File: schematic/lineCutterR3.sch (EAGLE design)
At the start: 60 parts, among them J1 10118192-0001LF, Q1 AO4576, Q2 AO4576, Q4 AO4576, Q5 DMG2305, SW1 KMR2, U1 MS560702BA03-50, U2 MDBT50Q, U3 S25FL128SDPMFIG13S03016, U4 ACS711KEXLT-31AB-T, U6 ICM-20602, X1 2x5 0.05"

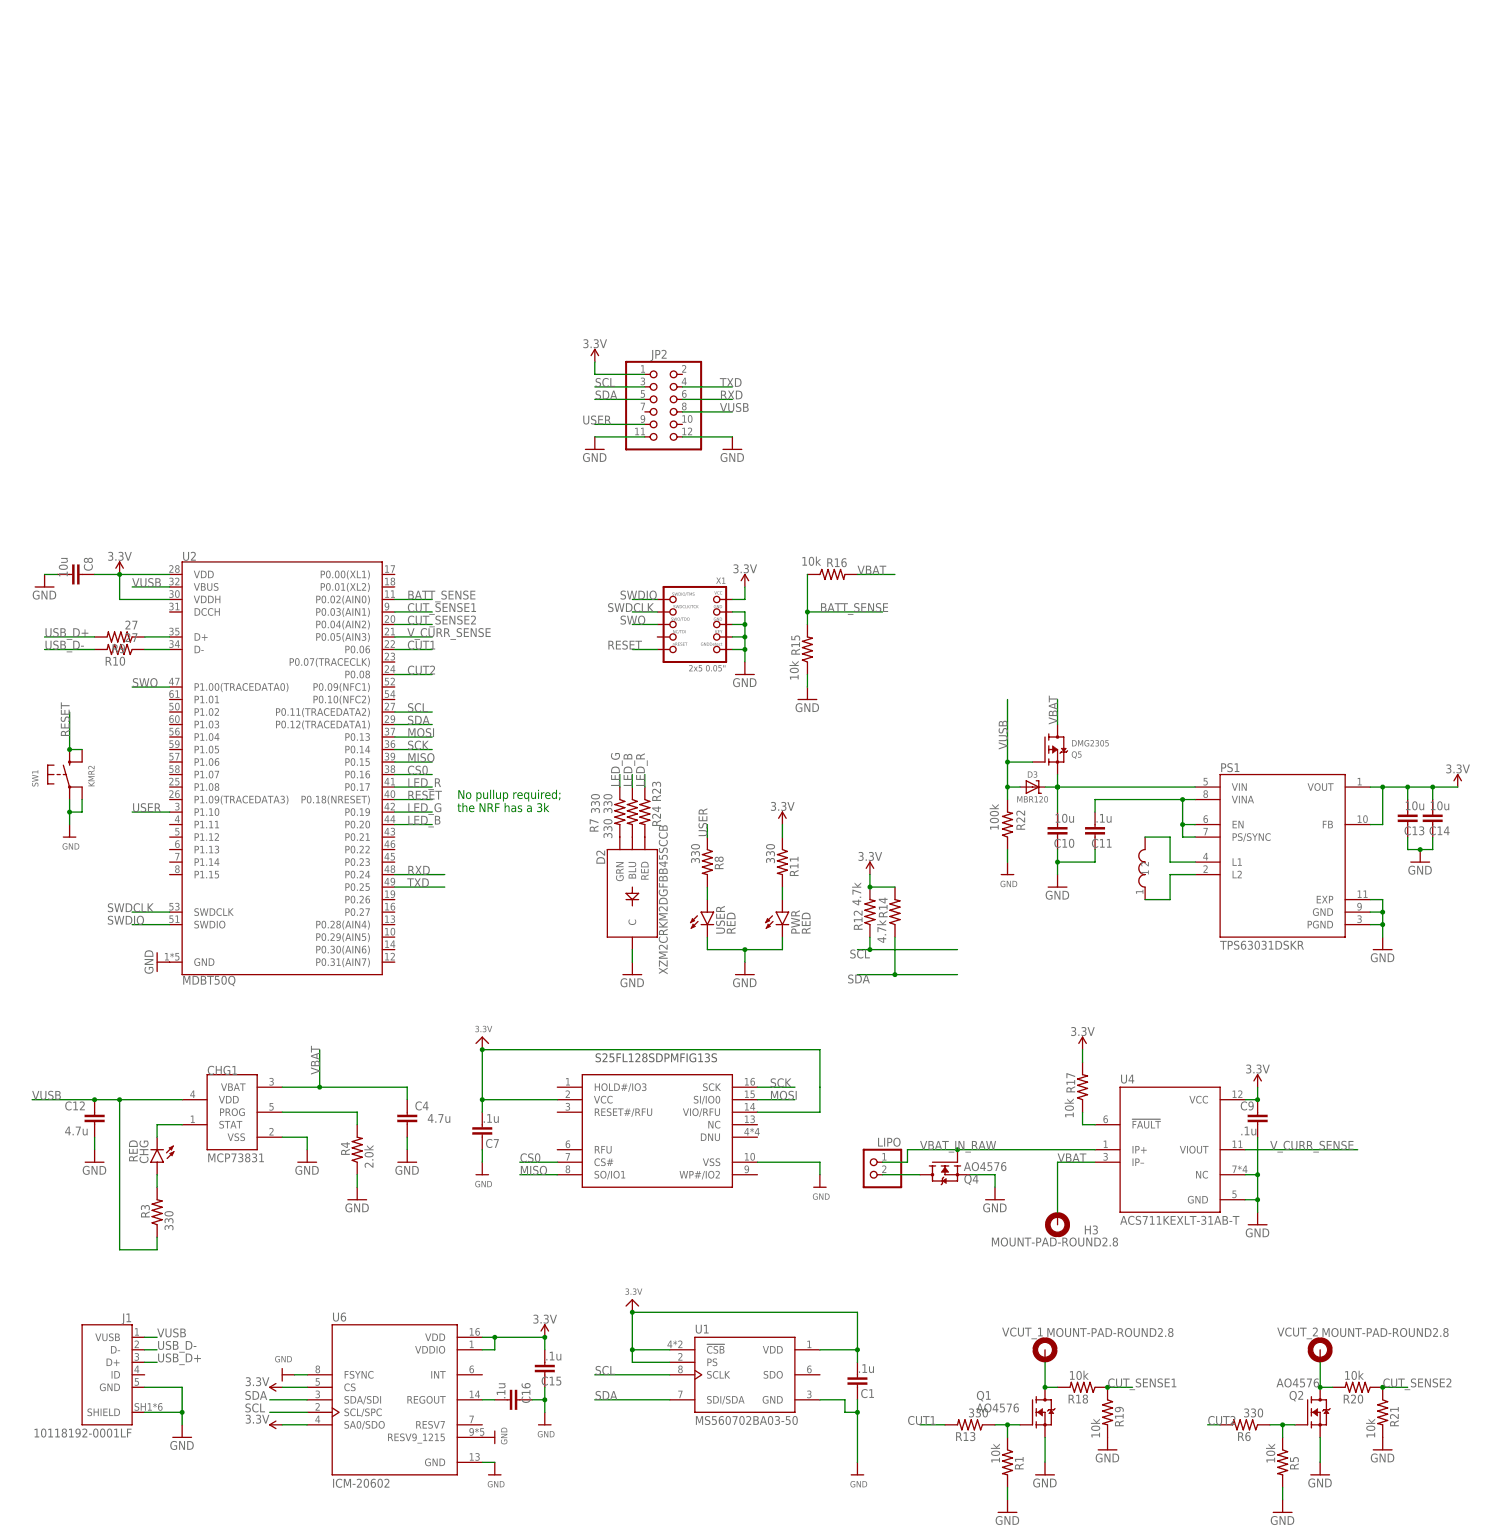
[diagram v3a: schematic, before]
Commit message: Switch back to 3v3 lin reg
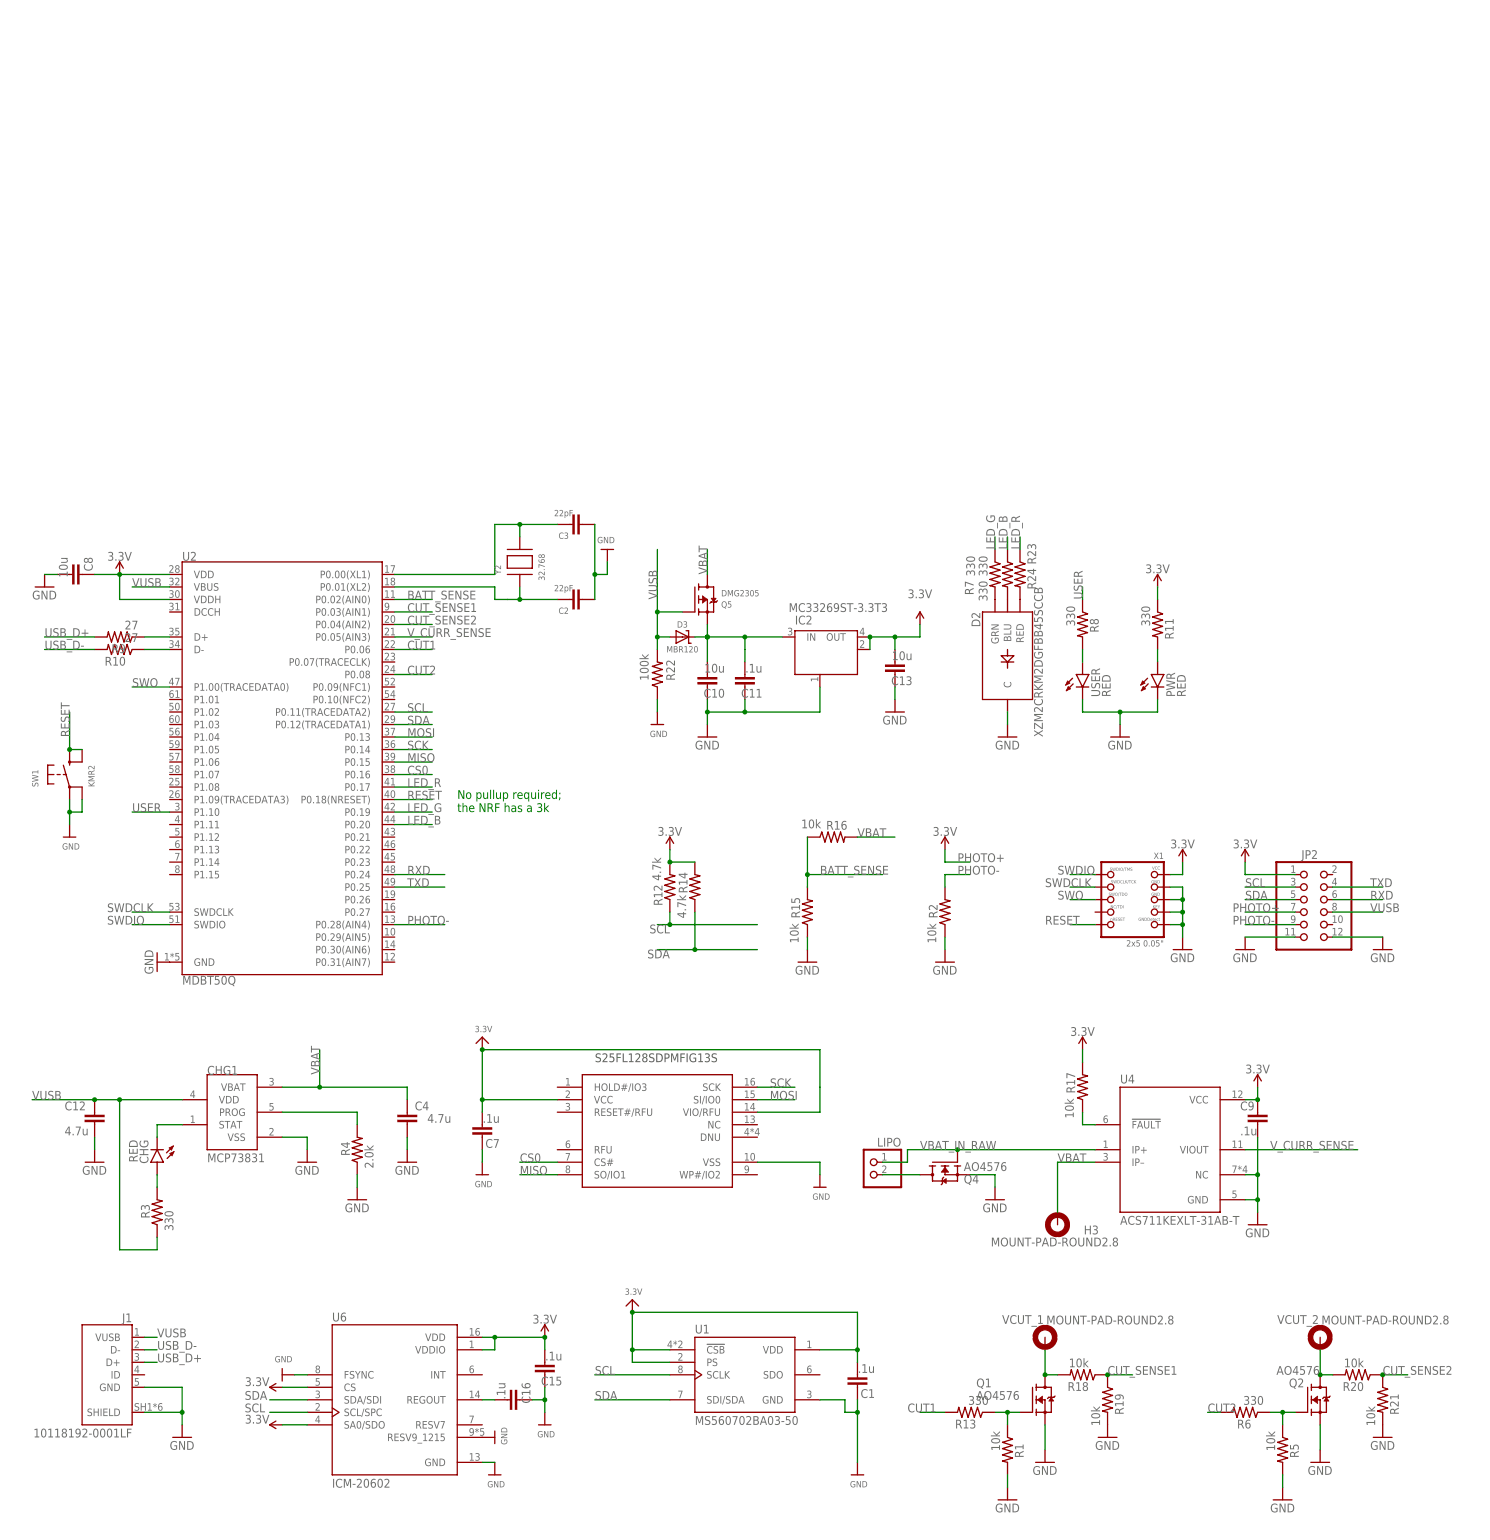
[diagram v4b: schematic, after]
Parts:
- removed C14: 10u, rcl:C-EUC0805
- removed L1: NR3015T1R5N, Line Cutter COTS:NR3015T1R5N
- removed PS1: TPS63031DSKR, Line Cutter COTS:TPS63031DSKR
- added C2, C3: 22pF, rcl:C-EUC0805
- added IC2: MC33269ST-3.3T3, linear:MC33269ST-3.3T3
- added R2: 10k, rcl:R-US_R0805
- added Y2: 32.768, adafruit2:XTAL-3.2X1.5
- H3, VCUT_1, VCUT_2: device holes:MOUNT-PAD-ROUND2.8 -> Line Cutter COTS:MOUNT-PAD-ROUND2.8
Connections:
- removed net N$18: C11.2, PS1.EN, PS1.PS/SYNC, PS1.VINA
- removed net N$19: L1.2, PS1.L1
- removed net N$20: L1.1, PS1.L2
- new net N$13: C3.1, U2.P0.00(XL1), Y2.P$2
- new net N$2: C2.1, U2.P0.01(XL2), Y2.P$1
- new net PHOTO+: JP2.7
- new net PHOTO-: JP2.9, R2.2, U2.P0.28(AIN4)
- net 3.3V: now also IC2.OUT, IC2.OUT@1; no longer C14.2, PS1.FB, PS1.VOUT
- net GND: now also C2.2, C3.2, IC2.GND/ADJ, R2.1; no longer C14.1, PS1.EXP, PS1.GND, PS1.PGND
- net USER: no longer JP2.9
- net VIN_REG1: now also C11.2, IC2.IN; no longer PS1.VIN
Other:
- moved on the sheet: C10, C11, C13, D2, D3, JP2, PWR, Q1, Q2, Q5, R1, R11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

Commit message: Final board stuff
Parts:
- U4: value ACS711KEXLT-31AB-T -> ACS711KEXLT-15AB-T
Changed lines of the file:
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@@
 <part name="GND22" library="supply1" library_urn="urn:adsk.eagle:library:371" deviceset="GND" device=""/>
 <part name="SUPPLY10" library="SparkFun-PowerSymbols" deviceset="3.3V" device=""/>
-<part name="U4" library="Line Cutter COTS" deviceset="ACS711KEXLT-31AB-T" device=""/>
+<part name="U4" library="Line Cutter COTS" deviceset="ACS711KEXLT-31AB-T" device="" value="ACS711KEXLT-15AB-T"/>
 <part name="D2" library="SparkFun-LED" deviceset="SUNLED" device="SMD1" value="XZM2CRKM2DGFBB45SCCB"/>
 <part name="GND7" library="supply1" library_urn="urn:adsk.eagle:library:371" deviceset="GND" device=""/>
